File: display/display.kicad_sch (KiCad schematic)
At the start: 4 parts, among them J2 Conn_02x05_Odd_Even, U1 D148K, U2 D148K, U3 D148K

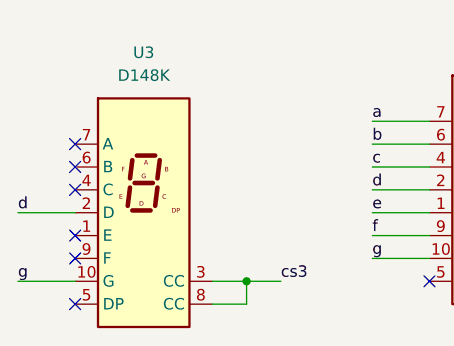
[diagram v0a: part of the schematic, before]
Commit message: display mod + plano
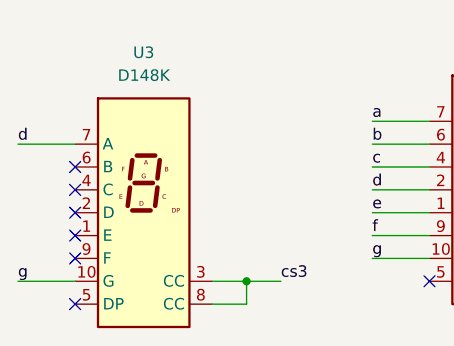
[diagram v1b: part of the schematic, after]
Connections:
- net d: now also U3.7 (A); no longer U3.2 (D)
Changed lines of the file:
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@@
   (junction (at 100.33 83.82) (diameter 0) (color 0 0 0 0)
   )
+  (no_connect (at 41.91 78.74))
   (no_connect (at 41.91 83.82))
-  (no_connect (at 41.91 71.12))
   (no_connect (at 81.28 86.36))
   (no_connect (at 41.91 76.2))
@@
     (stroke (width 0) (type default))
   )
-  (wire (pts (xy 35.56 78.74) (xy 41.91 78.74))
-    (stroke (width 0) (type default))
-  )
   (wire (pts (xy 111.76 83.82) (xy 118.11 83.82))
     (stroke (width 0) (type default))
@@
     (stroke (width 0) (type default))
   )
+  (wire (pts (xy 35.56 71.12) (xy 41.91 71.12))
+    (stroke (width 0) (type default))
+  )
   (wire (pts (xy 64.77 86.36) (xy 60.96 86.36))
     (stroke (width 0) (type default))
@@
   )
   (label "c" (at 74.93 73.66 0) (fields_autoplaced)
-    (effects (font (size 1.27 1.27)) (justify left bottom))
-  )
-  (label "d" (at 35.56 78.74 0) (fields_autoplaced)
     (effects (font (size 1.27 1.27)) (justify left bottom))
   )
@@
     (effects (font (size 1.27 1.27)) (justify left bottom))
   )
+  (label "d" (at 35.56 71.12 0) (fields_autoplaced)
+    (effects (font (size 1.27 1.27)) (justify left bottom))
+  )
